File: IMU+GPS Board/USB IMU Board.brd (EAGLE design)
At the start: 80 x 100 mm, 27 parts, among them IC1 MCP1703CB, J1 CON_HEADER_PRG_AVR_ICSP-SMD, Q1 12Mhz

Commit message: Finished with Rev.1
HW Layout done…
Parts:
- added JP2, JP3, JP4, JP5, JP6, JP7: (no value), SparkFun-Connectors:1X03
- added R5: 10K, SparkFun-Passives:0805
- added R6, R7: 2.2K, SparkFun-Passives:0805
- added U$7, U$8: FIDUCIAL, adafruit:FIDUCIAL_1MM
- added U$9: (no value), SparkFun-Aesthetics:OSHW-LOGO-L
- C5, C6: value (none) -> 12pF
- Q1: device adafruit:HC49UP -> crystal_3225:CRYSTAL-SMD-5X3
- Y1: value (none) -> 16 MHz
- moved J1 127.9 mm to (56.7, 22.0), turned to 270 degrees
- moved C10 103.1 mm to (36.4, 20.8)
- moved C6 102.0 mm to (44.5, 41.0), turned to 270 degrees
- moved C9 98.6 mm to (36.4, 18.3)
- moved C5 92.7 mm to (37.5, 41.0), turned to 270 degrees
- moved U$5 92.4 mm to (64.5, 9.50), turned to 90 degrees
- moved Y1 91.8 mm to (41.0, 41.0), turned to 180 degrees
- moved C4 91.0 mm to (49.3, 29.9), turned to 90 degrees
- moved R4 87.4 mm to (47.7, 39.0), turned to 180 degrees
- moved C8 84.7 mm to (26.0, 16.4), turned to 180 degrees
- moved C7 82.5 mm to (26.0, 19.4), turned to 180 degrees
- moved IC1 81.5 mm to (31.3, 17.9), turned to 90 degrees
- moved C3 76.0 mm to (40.7, 21.0), turned to 90 degrees
- moved C1 75.2 mm to (54.3, 15.0), turned to 180 degrees
- moved C2 66.8 mm to (40.7, 17.8), turned to 90 degrees
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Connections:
- net DIN+ renamed DIN_P
- net DIN- renamed DIN_N
- net USB1+ renamed USB1_P
- net USB1- renamed USB1_N
- removed net 5V: JP1.VBUS, U$3.P$47, U$5.P$1, U$6.P$1
- removed net USB2+: U$3.P$10, U$6.P$3
- removed net USB2-: U$3.P$9, U$6.P$2
- removed net USB3+: U$1.4, U$3.P$18
- removed net USB3-: U$1.3, U$3.P$17
- new net 1V8: R5.2, R6.1, R7.1, U$2.P$5
- new net GPS_RST: U$1.12, U$2.P$1
- new net N$10: R6.2, U$2.P$15
- new net N$11: R7.2, U$2.P$14
- new net N$8: R5.1, U$2.P$7
- new net ON_OFF: U$2.P$16, U$2.P$4
- new net RX: U$1.21, U$2.P$19
- new net TX: U$1.20, U$2.P$18
- new net USB2_N: U$1.3, U$3.P$9
- new net USB2_P: U$1.4, U$3.P$10
- new net USB3_N: U$3.P$17, U$6.P$2
- new net USB3_P: U$3.P$18, U$6.P$3
- net GND: now also Q1.2, Q1.4, U$2.GP$1, U$2.GP$10, U$2.GP$11, U$2.GP$12, U$2.GP$13, U$2.GP$14, U$2.GP$15, U$2.GP$16, U$2.GP$17, U$2.GP$18, U$2.GP$19, U$2.GP$2, U$2.GP$20, U$2.GP$21, U$2.GP$22, U$2.GP$23, U$2.GP$24, U$2.GP$3, U$2.GP$4, U$2.GP$5, U$2.GP$6, U$2.GP$7, U$2.GP$8, U$2.GP$9, U$2.P$6, U$2.P$9
- net N$6: now also Q1.3; no longer Q1.2
- net VCC: now also U$2.P$3
- net VUSB: now also JP1.VBUS, U$3.P$47, U$5.P$1, U$6.P$1
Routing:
- net VCC: track 0.00 -> 143.1 mm, vias 0 -> 3
- net VUSB: track 0.00 -> 129.7 mm, vias 0 -> 4
- net HUB_VCC: track 0.00 -> 51.6 mm
- net RX: track 0.00 -> 48.8 mm
- net TX: track 0.00 -> 48.1 mm
- net DIN_N: track 0.00 -> 43.6 mm
- net DIN_P: track 0.00 -> 43.4 mm
- net USB3_N: track 0.00 -> 42.8 mm
- net USB3_P: track 0.00 -> 42.7 mm
- net SDA: track 0.00 -> 39.7 mm, vias 0 -> 1
- net SCL: track 0.00 -> 36.8 mm, vias 0 -> 1
- net USB2_P: track 0.00 -> 34.0 mm
- net USB2_N: track 0.00 -> 33.9 mm
- net 1V8: track 0.00 -> 30.9 mm
- net RST: track 0.00 -> 30.1 mm, vias 0 -> 2
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- added copper zone on layer 1, net GND
- added copper zone on layer 16, net GND
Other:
- board size 80 x 100 mm -> 75 x 72 mm
- board text added: "Stereoscopic Imaging System USB Controller Board Vrakas Labs/SSI 2015 Rev.1"

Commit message: Rev 0.1bc1
Fixed some things, should be ready
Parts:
- added C11, C12: (no value), SparkFun-Capacitors:0805
- added LED1: GREEN, led:SML0805
- added LED2: RED, led:SML0805
- added R8, R9: 220, SparkFun-Resistors:0805
- C3: value 100n -> 100nF
- moved C7 1.20 mm to (24.8, 19.4)
- moved C8 1.20 mm to (24.8, 16.4)
- moved R2 0.50 mm to (41.3, 9.30)
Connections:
- new net N$12: LED1.A, R9.1
- new net N$13: LED2.A, R8.1
- new net N$14: R9.2, U$1.31
- new net N$15: R8.2, U$1.27
- net GND: now also C11.2, C12.2, LED1.C, LED2.C
- net VUSB: now also C11.1, C12.1
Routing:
- net VUSB: track 129.7 -> 134.8 mm
- net N$14: track 0.00 -> 4.43 mm
- net N$15: track 0.00 -> 4.00 mm
- net N$12: track 0.00 -> 2.87 mm
- net N$13: track 0.00 -> 2.35 mm
- net HUB_VCC: track 51.6 -> 53.4 mm
- net DIN_N: track 43.6 -> 42.4 mm
- net DIN_P: track 43.4 -> 42.4 mm
- net VCC: track 143.1 -> 143.6 mm
- net RESET: track 3.67 -> 4.22 mm

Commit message: Tore up USB junk
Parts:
- removed C1, C2: 20pF, SparkFun-Passives:0805
- removed Q1: 12Mhz, crystal_3225:CRYSTAL-SMD-5X3
- removed R1: 649, SparkFun-Passives:0805
- removed R2: 10K, SparkFun-Passives:0805
- removed R3: 100K, SparkFun-Passives:0805
- removed U$3: CY7C65642, NASA Parts Lib:TQFP-48
- removed U$5, U$6: USB-SOCKET, NASA Parts Lib:TE-1932854-1-USB
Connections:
- removed net HUB_VCC: R2.2, R3.2, U$3.P$1, U$3.P$12, U$3.P$16, U$3.P$19, U$3.P$25, U$3.P$34, U$3.P$38, U$3.P$44, U$3.P$48, U$3.P$7
- removed net N$1: R1.2, U$3.P$11
- removed net N$2: R3.1, U$3.P$39
- removed net N$4: C1.2, Q1.1, U$3.P$14
- removed net N$6: C2.2, Q1.3, U$3.P$15
- removed net RESET: R2.1, U$3.P$26
- removed net USB1_N: U$3.P$5, U$5.P$2
- removed net USB1_P: U$3.P$6, U$5.P$3
- removed net USB3_N: U$3.P$17, U$6.P$2
- removed net USB3_P: U$3.P$18, U$6.P$3
- net DIN_N: no longer U$3.P$3
- net DIN_P: no longer U$3.P$4
- net GND: no longer C1.1, C2.1, Q1.2, Q1.4, R1.1, U$3.P$13, U$3.P$2, U$3.P$20, U$3.P$27, U$3.P$37, U$3.P$8, U$5.G$1, U$5.G$2, U$5.G$3, U$5.G$4, U$5.P$4, U$6.G$1, U$6.G$2, U$6.G$3, U$6.G$4, U$6.P$4
- net USB2_N: no longer U$3.P$9
- net USB2_P: no longer U$3.P$10
- net VUSB: no longer U$3.P$47, U$5.P$1, U$6.P$1
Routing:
- net HUB_VCC: track 53.4 -> 0.00 mm
- net USB3_N: track 42.8 -> 0.00 mm
- net USB3_P: track 42.7 -> 0.00 mm
- net USB1_N: track 12.8 -> 0.00 mm
- net USB1_P: track 12.7 -> 0.00 mm
- net VUSB: track 134.8 -> 122.6 mm
- net N$4: track 12.1 -> 0.00 mm
- net N$6: track 11.6 -> 0.00 mm
- net USB2_N: track 34.1 -> 28.4 mm
- net USB2_P: track 34.1 -> 28.6 mm
- net RESET: track 4.22 -> 0.00 mm
- net N$1: track 3.05 -> 0.00 mm
- net N$2: track 2.75 -> 0.00 mm
- net DIN_P: track 42.4 -> 40.9 mm
- net DIN_N: track 42.4 -> 41.1 mm

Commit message: First Round of new board
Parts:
- removed C11, C12: (no value), SparkFun-Capacitors:0805
- removed JP2, JP6: (no value), SparkFun-Connectors:1X03
- added D1: (no value), SparkFun-DiscreteSemi:SMA-DIODE
- added LED3: BLUE, led:SML0805
- added R1: 220, SparkFun-Resistors:0805
- added R2: 10K, SparkFun-Resistors:0805
- added S1: (no value), SparkFun-Electromechanical:SWITCH-SPDT
- added SW1: (no value), SparkFun-Electromechanical:TACTILE-SWITCH-SMD
- added U$3: 3V, NASA Parts Lib:BU2032SM-G
- Y1: value 16 MHz -> 16Mhz
- moved U$7 65.4 mm to (67.5, 67.5)
- moved FRAME1 63.5 mm to (61.1, 17.2)
- moved U$4 46.4 mm to (21.0, 69.6), turned to 180 degrees
- moved LED2 45.3 mm to (63.2, 3.90), turned to 90 degrees
- moved JP7 41.0 mm to (62.0, 21.0)
- moved LED1 40.8 mm to (66.2, 3.90), turned to 90 degrees
- moved R9 40.0 mm to (66.2, 8.30)
- moved R8 39.6 mm to (63.2, 8.30), turned to 90 degrees
- moved JP4 34.8 mm to (44.0, 41.0)
- moved U$9 33.3 mm to (49.6, 28.8)
- moved R6 32.5 mm to (35.2, 43.5)
- moved R4 30.6 mm to (25.7, 17.7), turned to 0 degrees
- moved R7 30.6 mm to (41.9, 44.4)
- moved R5 30.2 mm to (26.7, 52.5)
- moved U$2 29.9 mm to (29.7, 45.5)
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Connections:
- removed net N$14: R9.2, U$1.31
- removed net N$15: R8.2, U$1.27
- removed net USB2_N: U$1.3
- removed net USB2_P: U$1.4
- new net 3V3IN: D1.C, IC1.2, S1.2
- new net LED1: R9.2, U$1.27
- new net LED2: R8.2, U$1.26
- new net N$4: LED3.A, R1.2
- new net N$5: D1.A, U$3.PVCC
- new net PWRBTN: R2.2, SW1.1, SW1.2, U$1.28
- net DIN_N: now also U$1.3
- net DIN_P: now also U$1.4
- net GND: now also LED3.C, SW1.3, SW1.4, U$3.PGND; no longer C11.2, C12.2
- net VCC: now also R1.1, R2.1, S1.3; no longer IC1.2, J1.2
- net VUSB: now also J1.2; no longer C11.1, C12.1
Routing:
- net 3V3IN: track 0.00 -> 136.2 mm, vias 0 -> 2
- net GPS_RST: track 20.4 -> 57.2 mm
- net LED1: track 0.00 -> 35.6 mm
- net LED2: track 0.00 -> 31.8 mm
- net PWRBTN: track 0.00 -> 31.0 mm, vias 0 -> 2
- net USB2_P: track 28.6 -> 0.00 mm
- net USB2_N: track 28.4 -> 0.00 mm
- net VUSB: track 122.6 -> 99.5 mm
- net SCL: track 36.8 -> 56.0 mm
- net SCK: track 17.7 -> 36.2 mm
- net N$2: track 9.90 -> 25.8 mm
- net MOSI: track 23.7 -> 39.0 mm
- net VCC: track 143.6 -> 155.7 mm, vias 3 -> 8
- net SDA: track 39.7 -> 50.7 mm
- net MISO: track 16.8 -> 27.7 mm
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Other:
- board size 75 x 72 mm -> 70 x 70 mm
- board text added: "ON OFF"
- board text added: "Stereoscopic Imaging System USB Sensor Board Vrakas Labs/SSI 2016 Rev.2"
- board text removed: "Stereoscopic Imaging System USB Controller Board Vrakas Labs/SSI 2015 Rev.1"

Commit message: Rev 0.2bc1 (todo: Hand Review)
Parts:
- LED1: value GREEN -> GR
- LED2: value RED -> RD
- LED3: value BLUE -> BL
- moved D1 8.14 mm to (53.9, 59.8), turned to 270 degrees
- moved LED3 2.19 mm to (58.7, 5.50)
- moved LED1 2.06 mm to (67.5, 5.50)
- moved R1 2.00 mm to (60.2, 10.3)
- moved R8 2.00 mm to (63.2, 10.3)
- moved R9 2.00 mm to (66.2, 10.3)
- moved LED2 1.63 mm to (63.5, 5.50)
- moved U$7 0.71 mm to (68.0, 68.0)
- moved U$4 0.20 mm to (21.0, 69.4)
- renumbered J1 to ICSP, SW1 to SHUTDOWN
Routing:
- net 3V3IN: track 136.2 -> 124.8 mm
- net N$5: track 6.07 -> 8.80 mm
- net VCC: track 155.7 -> 153.7 mm
- net LED2: track 31.8 -> 29.8 mm
- net LED1: track 35.6 -> 33.6 mm
- net N$4: track 2.45 -> 3.47 mm
- net N$12: track 2.45 -> 3.39 mm
- net VUSB: track 99.5 -> 100.4 mm
- net PWRBTN: track 31.0 -> 31.7 mm
- net N$13: track 2.45 -> 2.97 mm
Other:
- outline, holes or cut-outs redrawn
- board text added: "ALWAYS press SHUTDOWN and wait for PWR LED to flash before switching off"
- board text added: "GPS"
- board text added: "IO"
- board text added: "PWR"

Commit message: Late Night
Needs Check
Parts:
- removed C7: 1uF, SparkFun-Passives:0805
- removed C8: 100nF, SparkFun-Passives:0805
- removed D1: (no value), SparkFun-DiscreteSemi:SMA-DIODE
- removed IC1: MCP1703CB, linear:SOT23
- removed R2: 10K, SparkFun-Resistors:0805
- removed R5: 10K, SparkFun-Passives:0805
- removed R6, R7: 2.2K, SparkFun-Passives:0805
- removed S1: (no value), SparkFun-Electromechanical:SWITCH-SPDT
- removed SHUTDOWN: (no value), SparkFun-Electromechanical:TACTILE-SWITCH-SMD
- removed U$2: A2235-H, NASA Parts Lib:A2235-H
- removed U$3: 3V, NASA Parts Lib:BU2032SM-G
- added C1: 1uF, SparkFun-Passives:0805
- added C2: 100nF, SparkFun-Passives:0805
- added J1: Adafruit GPS, SparkFun-Connectors:1X09
- added RESET: RST, SparkFun-Electromechanical:TACTILE-SWITCH-SMD
- R1, R8, R9: value 220 -> 330
- moved FRAME1 63.5 mm to (0.00, 0.00)
- moved U$9 44.6 mm to (5.37, 34.9)
- moved U$8 29.0 mm to (2.00, 2.00)
- moved ICSP 27.0 mm to (24.1, 6.20), turned to 180 degrees
- moved C6 23.0 mm to (32.6, 11.8), turned to 90 degrees
- moved LED1 15.7 mm to (51.8, 5.50)
- moved LED2 15.7 mm to (47.8, 5.50)
- moved LED3 15.7 mm to (43.0, 5.50)
- moved R1 15.7 mm to (44.5, 10.3)
- moved R8 15.7 mm to (47.5, 10.3)
- moved R9 15.7 mm to (50.5, 10.3)
- moved U$7 15.0 mm to (53.0, 68.0)
- moved Y1 14.5 mm to (36.9, 11.9), turned to 0 degrees
- moved JP7 14.0 mm to (48.0, 21.0)
- moved C5 6.02 mm to (41.6, 13.6), turned to 180 degrees
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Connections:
- removed net 1V8: R5.2, R6.1, R7.1, U$2.P$5
- removed net 3V3IN: D1.C, IC1.2, S1.2
- removed net GPS_RST: U$1.12, U$2.P$1
- removed net N$10: R6.2, U$2.P$15
- removed net N$11: R7.2, U$2.P$14
- removed net N$5: D1.A, U$3.PVCC
- removed net N$8: R5.1, U$2.P$7
- removed net ON_OFF: U$2.P$16, U$2.P$4
- removed net PWRBTN: R2.2, SHUTDOWN.1, SHUTDOWN.2, U$1.28
- removed net RX: U$1.21, U$2.P$19
- removed net TX: U$1.20, U$2.P$18
- removed net VUSB: C7.1, C8.1, IC1.3, ICSP.2, JP1.VBUS, U$1.2, U$1.7
- new net GPS_EN: J1.2, U$1.36
- new net MIGO: J1.5, U$1.20
- new net MOGI: J1.6, U$1.21
- net GND: now also C1.2, C2.2, J1.7, RESET.3, RESET.4; no longer C7.2, C8.2, IC1.1, SHUTDOWN.3, SHUTDOWN.4, U$2.GP$1, U$2.GP$10, U$2.GP$11, U$2.GP$12, U$2.GP$13, U$2.GP$14, U$2.GP$15, U$2.GP$16, U$2.GP$17, U$2.GP$18, U$2.GP$19, U$2.GP$2, U$2.GP$20, U$2.GP$21, U$2.GP$22, U$2.GP$23, U$2.GP$24, U$2.GP$3, U$2.GP$4, U$2.GP$5, U$2.GP$6, U$2.GP$7, U$2.GP$8, U$2.GP$9, U$2.P$6, U$2.P$9, U$3.PGND
- net RST: now also RESET.1, RESET.2
- net VCC: now also C1.1, C2.1, ICSP.2, J1.8, JP1.VBUS, U$1.2, U$1.7; no longer R2.1, S1.3, U$2.P$3
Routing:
- net 3V3IN: track 124.8 -> 0.00 mm, vias 2 -> 0
- net VUSB: track 100.4 -> 0.00 mm, vias 4 -> 0
- net RX: track 58.9 -> 0.00 mm, vias 2 -> 0
- net MIGO: track 0.00 -> 57.3 mm, vias 0 -> 1
- net GPS_RST: track 57.2 -> 0.00 mm, vias 2 -> 0
- net TX: track 56.2 -> 0.00 mm, vias 2 -> 0
- net GPS_EN: track 0.00 -> 54.8 mm, vias 0 -> 1
- net MOGI: track 0.00 -> 48.6 mm, vias 0 -> 1
- net 1V8: track 32.2 -> 0.00 mm
- net PWRBTN: track 31.7 -> 0.00 mm, vias 2 -> 0
- net ON_OFF: track 24.3 -> 0.00 mm
- net N$10: track 22.1 -> 0.00 mm
- net SCK: track 36.2 -> 17.6 mm
- net LED1: track 33.6 -> 15.2 mm
- net MOSI: track 39.0 -> 22.0 mm
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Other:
- board size 70 x 70 mm -> 55 x 70 mm
- board text added: "USB Sensor Board Vrakas Labs/SSI 2016 Rev.3"
- board text removed: "ALWAYS press SHUTDOWN and wait for PWR LED to flash before switching off"
- board text removed: "ON OFF"
- board text removed: "Stereoscopic Imaging System USB Sensor Board Vrakas Labs/SSI 2016 Rev.2"

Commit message: v3 Board Run
No going back now!
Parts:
- removed FRAME1: FRAME-LETTERNO_PACKAGE, SparkFun-Aesthetics:DUMMY
- moved R4 9.14 mm to (18.2, 11.6)
- moved C4 3.23 mm to (26.2, 18.6)
- moved C3 1.00 mm to (35.0, 31.8)
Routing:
- net VCC: track 150.6 -> 155.9 mm, vias 4 -> 3
- net N$9: track 2.91 -> 6.32 mm
- net RST: track 38.2 -> 40.1 mm
- net N$3: track 2.80 -> 3.80 mm
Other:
- outline, holes or cut-outs redrawn

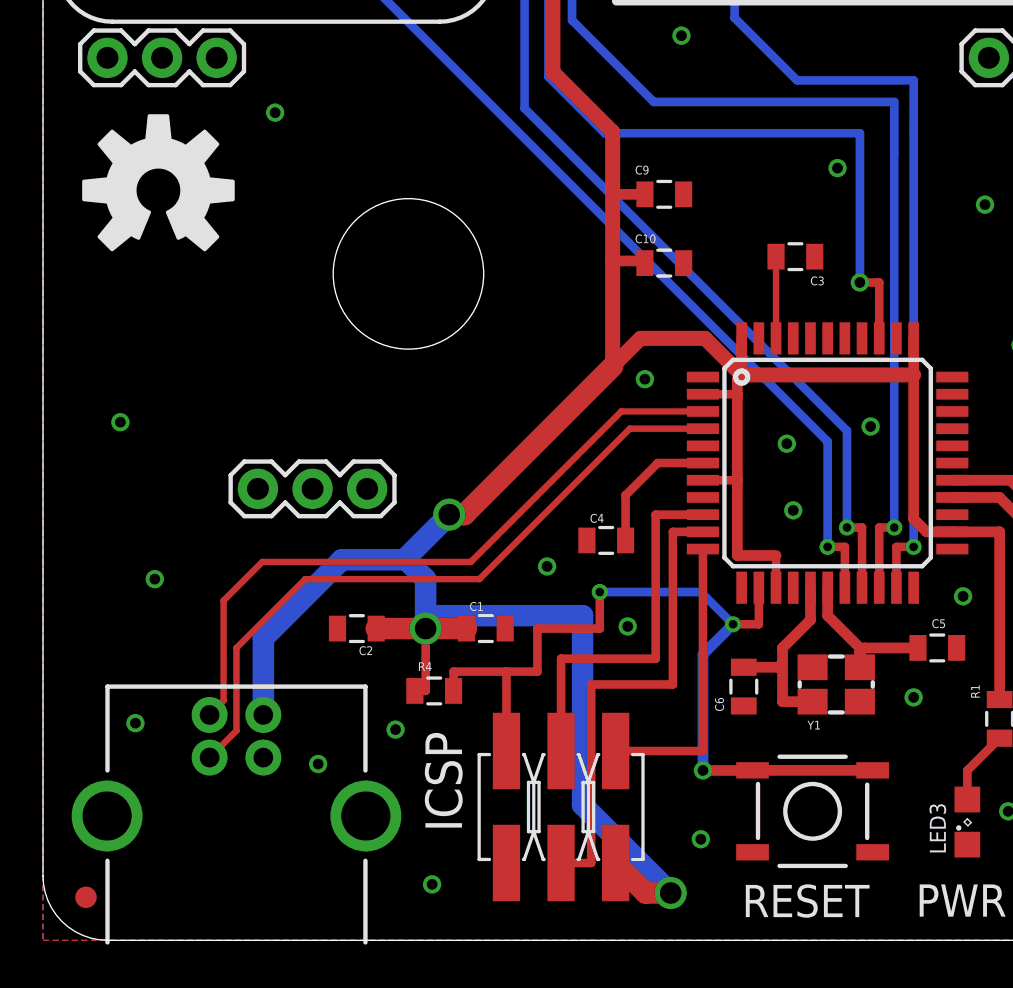
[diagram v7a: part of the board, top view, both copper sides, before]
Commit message: USB traces now Impedance Matched
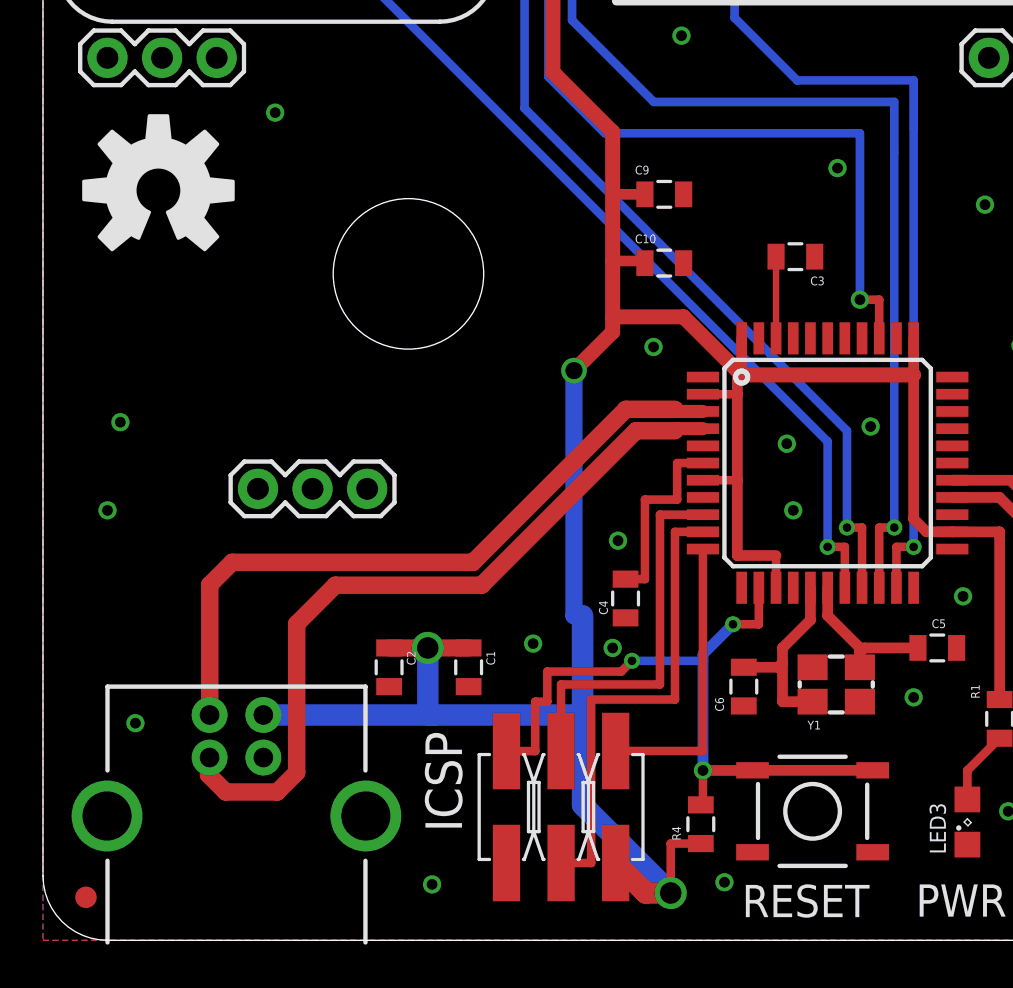
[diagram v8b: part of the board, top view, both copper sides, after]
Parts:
- moved R4 13.9 mm to (30.6, 5.40), turned to 90 degrees
- moved C4 2.85 mm to (27.1, 15.9), turned to 90 degrees
- moved C2 2.34 mm to (16.1, 12.7), turned to 270 degrees
- moved C1 1.97 mm to (19.8, 12.7), turned to 270 degrees
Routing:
- net VCC: track 155.9 -> 147.3 mm
- net RST: track 40.1 -> 32.9 mm
- net DIN_P: track 31.5 -> 35.2 mm
- net N$9: track 6.32 -> 9.00 mm
- net DIN_N: track 31.5 -> 32.4 mm
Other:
- board text added: "USB Sensor Board Vrakas Labs/SSI 2016 Rev.3b"
- board text removed: "USB Sensor Board Vrakas Labs/SSI 2016 Rev.3"
